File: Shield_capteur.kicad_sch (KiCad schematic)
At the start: 21 parts, among them J1 Power, J2 Digital/PWM, J3 Analog, J4 Digital/PWM, J5 Conn_01x02_Pin, K63 1uF, U1 LTC1050ACN8_PBF, U2 MCP

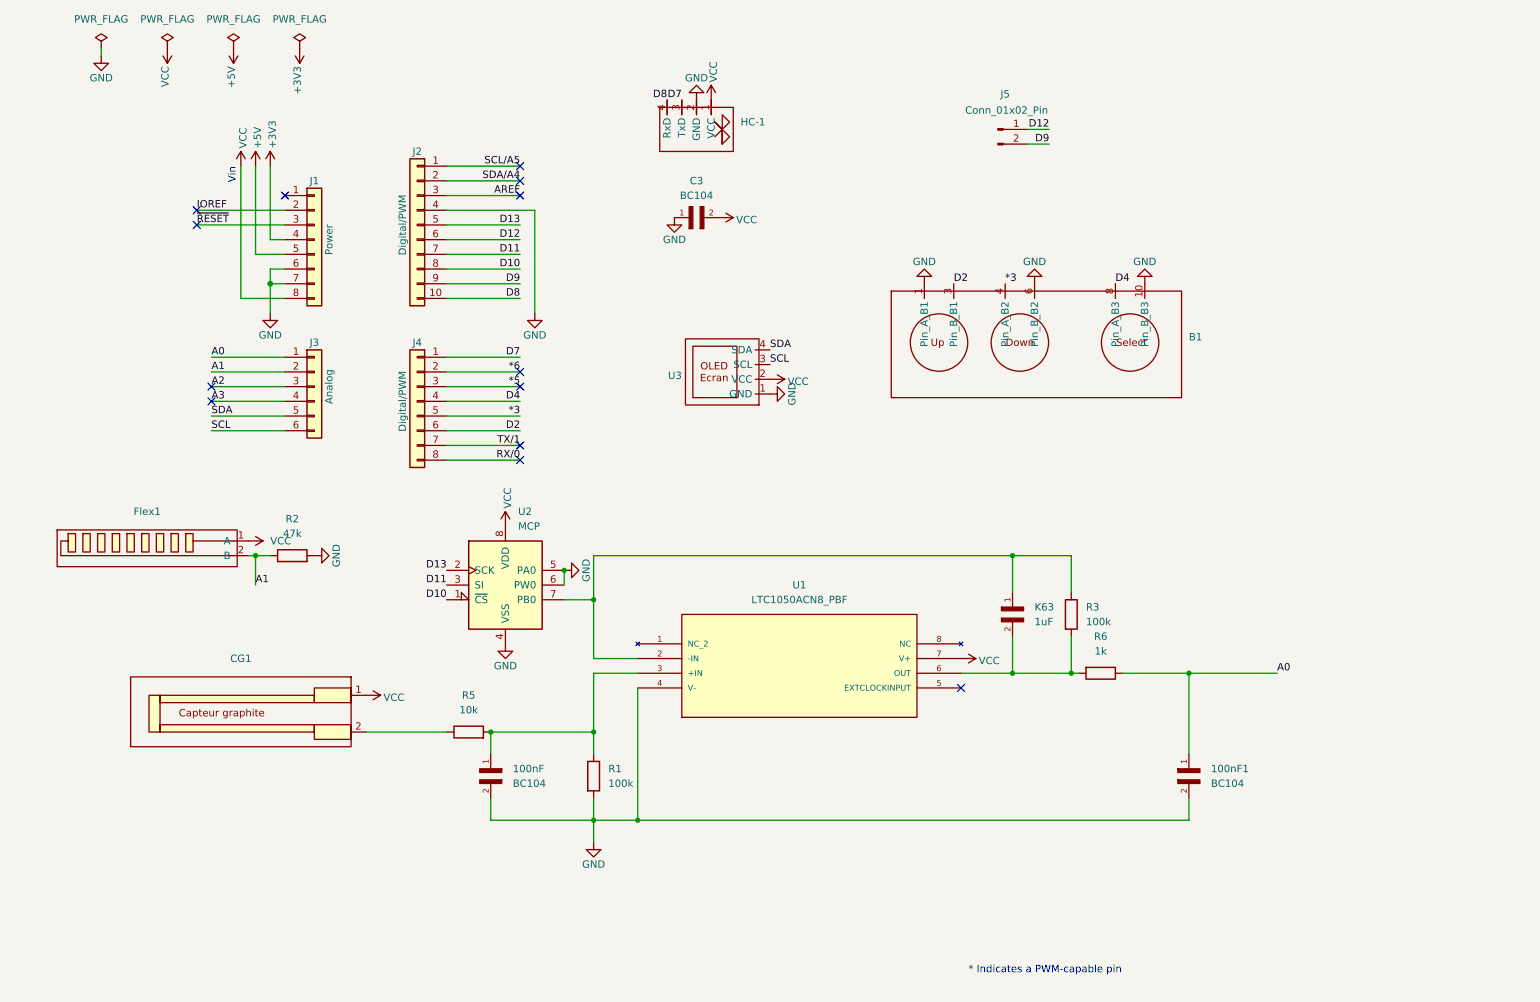
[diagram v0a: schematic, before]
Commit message: Mise en forme shematic et rajout valeurs MCP
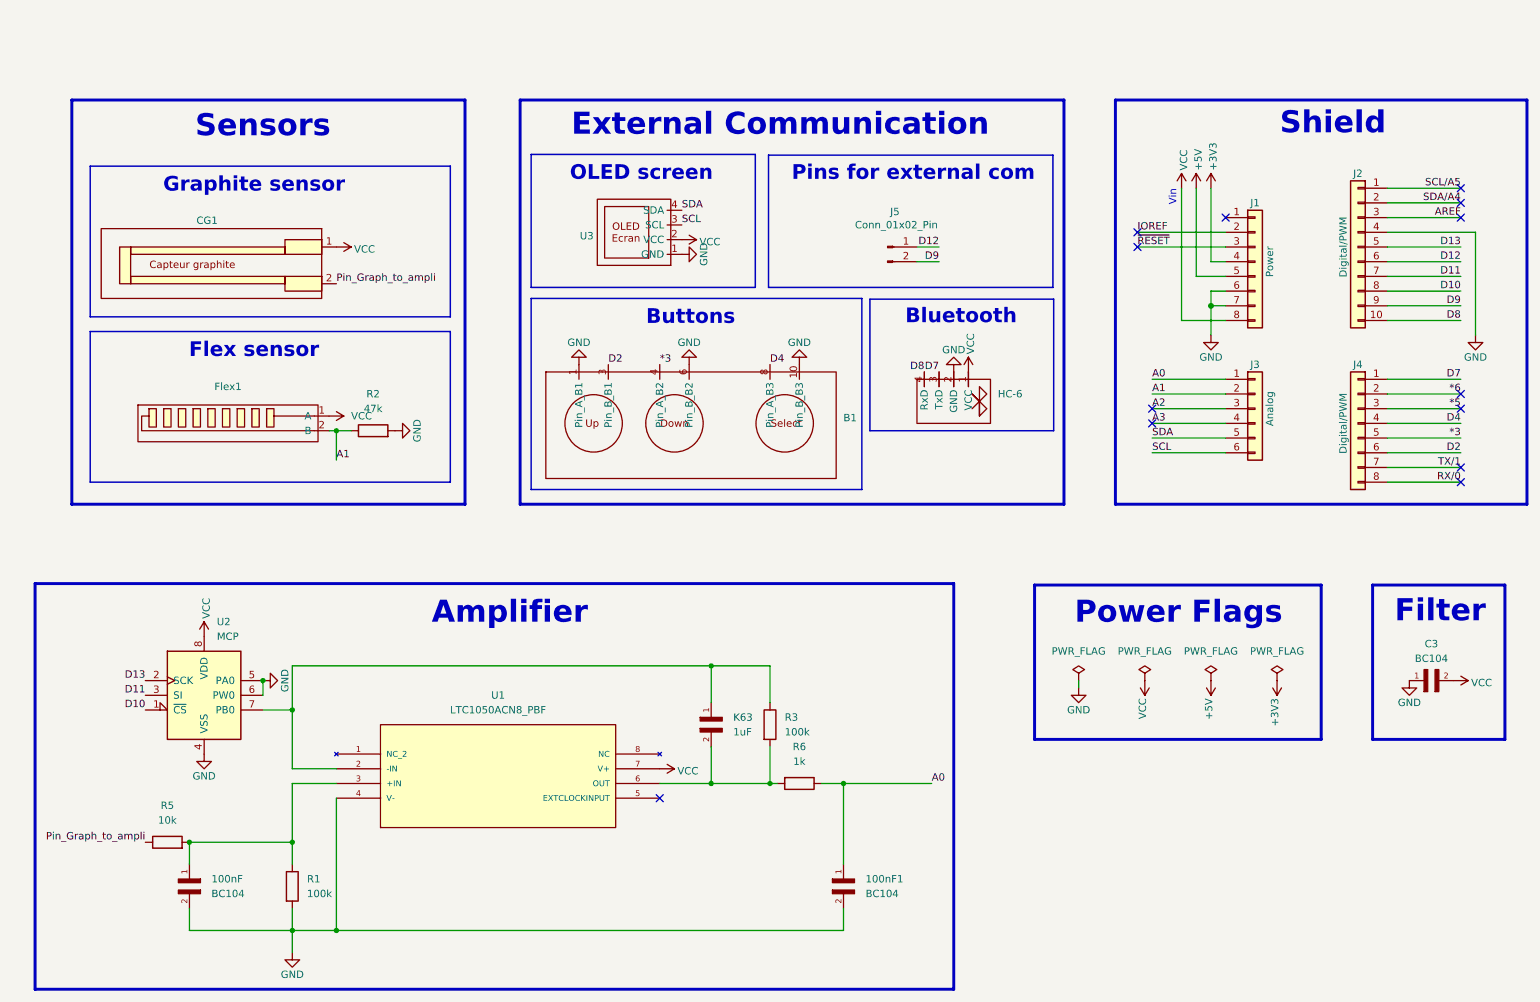
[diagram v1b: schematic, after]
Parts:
- renumbered HC-1 to HC-6
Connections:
- net Pin_Graph_to_ampli: now reaches CG1.2, R5.1
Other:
- note added: "Amplifier"
- note added: "Bluetooth"
- note added: "Buttons"
- note added: "External Communication"
- note added: "Filter"
- note added: "Flex sensor"
- note added: "Graphite sensor"
- note added: "OLED screen"
- note added: "Pins for external com"
- note added: "Power Flags"
- note added: "Sensors"
- note added: "Shield"
- note removed: "* Indicates a PWM-capable pin"
- title: Demo_board -> Projet Graphite sensor
- moved on the sheet: 100nF1, B1, BC104, C3, CG1, Flex1, HC-6, J1, J2, J3, J4, J5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
